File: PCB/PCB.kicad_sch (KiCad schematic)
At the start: 148 parts, among them J1 USB_C_Receptacle_USB2.0_16P, J2 Battery, J3 Conn_01x04, J4 Conn_01x05, Q1 AO3401A, Q2 2N7002, Q3 2N7002, SW1 SW_Push, SW10 MX_SW_HS, SW11 MX_SW_HS, SW12 MX_SW_HS, SW13 MX_SW_HS, SW14 MX_SW_HS, SW15 MX_SW_HS, SW16 MX_SW_HS, SW17 MX_SW_HS, SW18 MX_SW_HS, SW19 MX_SW_HS, SW2 MX_SW_HS, SW20 MX_SW_HS, SW21 MX_SW_HS, SW22 MX_SW_HS, SW23 MX_SW_HS, SW24 MX_SW_HS, SW25 MX_SW_HS, SW26 MX_SW_HS, SW27 MX_SW_HS, SW28 MX_SW_HS, SW29 MX_SW_HS, SW3 MX_SW_HS, SW30 SW_SPDT, SW31 MX_SW_HS, SW32 MX_SW_HS, SW33 MX_SW_HS, SW34 MX_SW_HS, SW35 MX_SW_HS, SW36 MX_SW_HS, SW37 MX_SW_HS, SW4 MX_SW_HS, SW5 MX_SW_HS, SW6 MX_SW_HS, SW7 MX_SW_HS, SW8 MX_SW_HS, SW9 MX_SW_HS, U1 MAX17048, U2 DW01A, U3 FS8205, U4 BQ24075RGT, U5 nRF52840_E73-2G4M08S1C, Y1 32.768 KHz

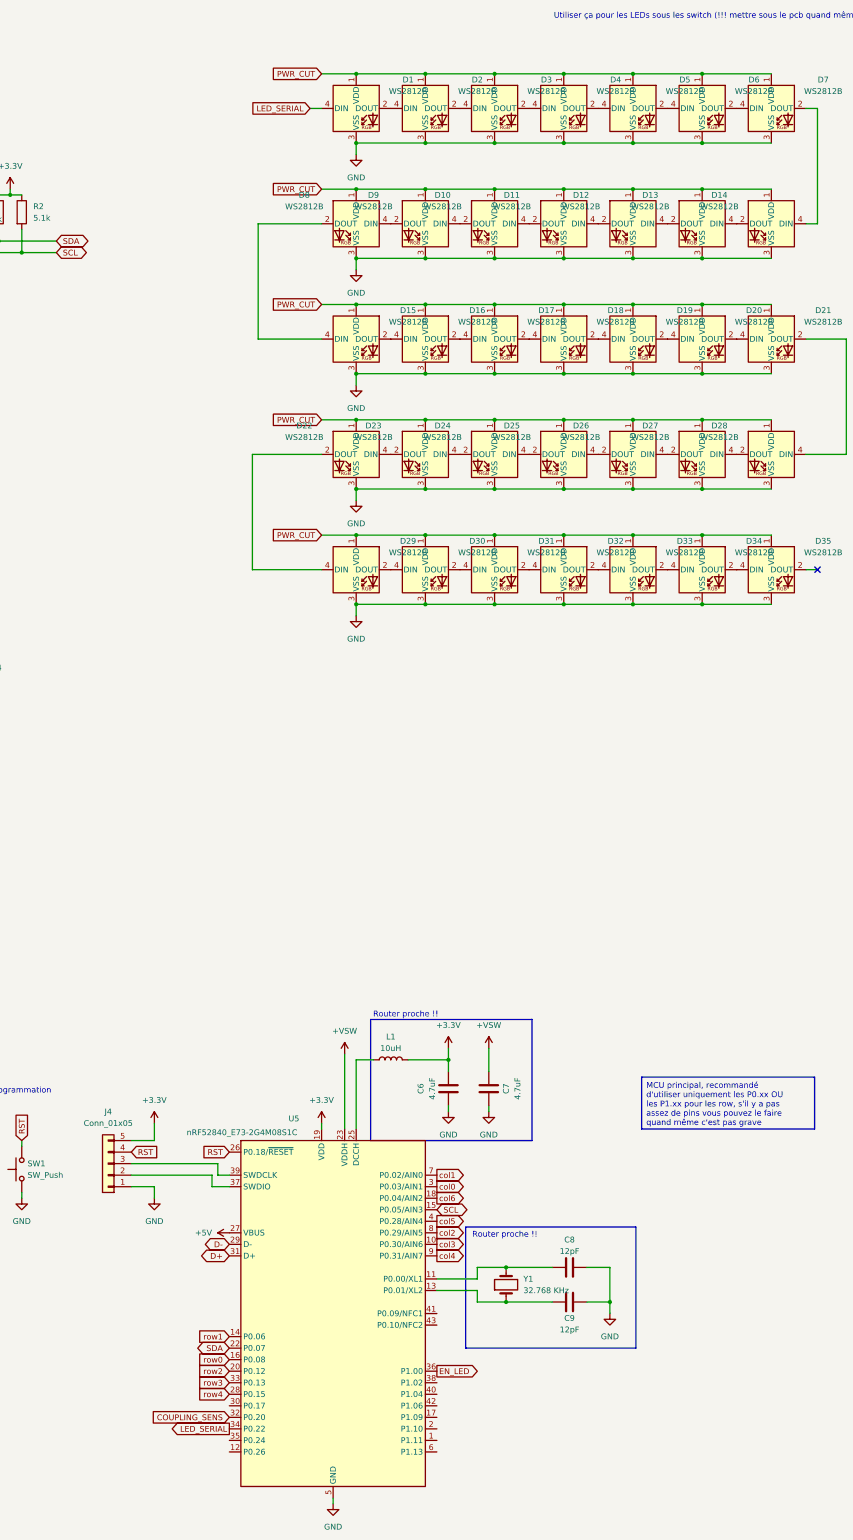
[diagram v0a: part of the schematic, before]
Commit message: Tried LEDs, too complicated
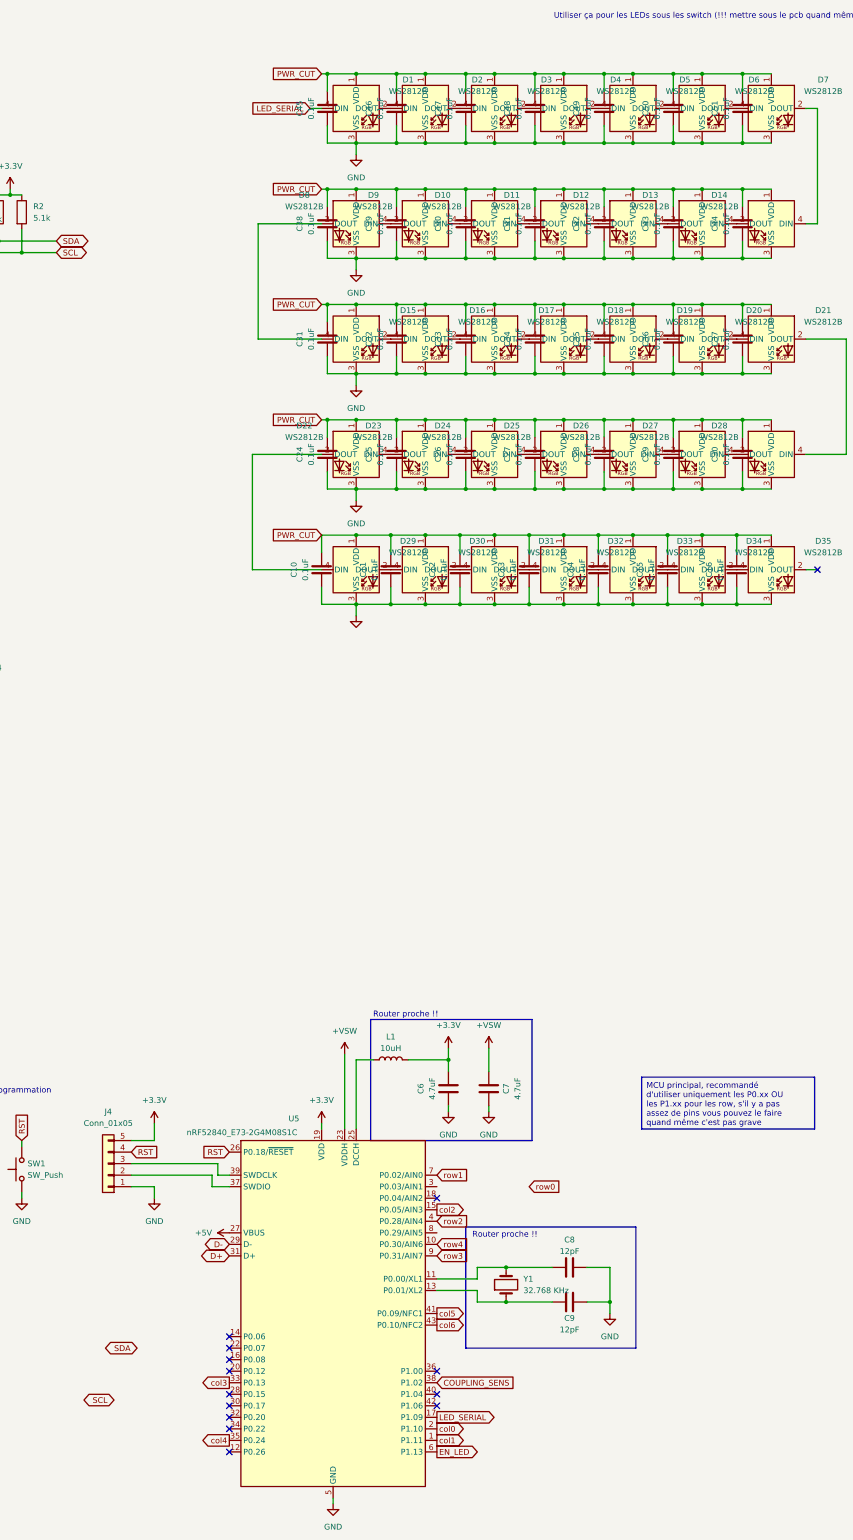
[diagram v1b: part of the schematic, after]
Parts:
- added C10, C11, C12, C13, C14, C15, C16, C24, C25, C26, C27, C28, C29, C30, C31, C32, C33, C34, C35, C36, C37, C38, C39, C40, C41, C42, C43, C44, C45, C46, C47, C48, C49, C50, C51: 0.1uF, Capacitor_SMD:C_0603_1608Metric_Pad1.08x0.95mm_HandSolder, symbol Device:C
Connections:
- net COUPLING_SENS: now also U5.38 (P1.02); no longer U5.32 (P0.20)
- net EN_LED: now also U5.6 (P1.13); no longer U5.36 (P1.00)
- net GND: now also C10.1, C11.1, C12.1, C13.1, C14.1, C15.1, C16.1, C24.1, C25.1, C26.1, C27.1, C28.1, C29.1, C30.1, C31.1, C32.1, C33.1, C34.1, C35.1, C36.1, C37.1, C38.1, C39.1, C40.1, C41.1, C42.1, C43.1, C44.1, C45.1, C46.1, C47.1, C48.1, C49.1, C50.1, C51.1
- net LED_SERIAL: now also U5.17 (P1.09); no longer U5.34 (P0.22)
- net PWR_CUT: now also C10.2, C11.2, C12.2, C13.2, C14.2, C15.2, C16.2, C24.2, C25.2, C26.2, C27.2, C28.2, C29.2, C30.2, C31.2, C32.2, C33.2, C34.2, C35.2, C36.2, C37.2, C38.2, C39.2, C40.2, C41.2, C42.2, C43.2, C44.2, C45.2, C46.2, C47.2, C48.2, C49.2, C50.2, C51.2
- net SCL: no longer U5.15 (P0.05/AIN3)
- net SDA: no longer U5.22 (P0.07)
- net col0: now also U5.2 (P1.10); no longer U5.3 (P0.03/AIN1)
- net col1: now also U5.1 (P1.11); no longer U5.7 (P0.02/AIN0)
- net col2: now also U5.15 (P0.05/AIN3); no longer U5.8 (P0.29/AIN5)
- net col3: now also U5.33 (P0.13); no longer U5.10 (P0.30/AIN6)
- net col4: now also U5.35 (P0.24); no longer U5.9 (P0.31/AIN7)
- net col5: now also U5.41 (P0.09/NFC1); no longer U5.4 (P0.28/AIN4)
- net col6: now also U5.43 (P0.10/NFC2); no longer U5.18 (P0.04/AIN2)
- net row0: no longer U5.16 (P0.08)
- net row1: now also U5.7 (P0.02/AIN0); no longer U5.14 (P0.06)
- net row2: now also U5.4 (P0.28/AIN4); no longer U5.20 (P0.12)
- net row3: now also U5.9 (P0.31/AIN7); no longer U5.33 (P0.13)
- net row4: now also U5.10 (P0.30/AIN6); no longer U5.28 (P0.15)
- no-connect marks 7 -> 20
